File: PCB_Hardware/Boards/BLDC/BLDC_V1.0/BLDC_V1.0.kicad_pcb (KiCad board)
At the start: 4 copper layers, 60 x 60 mm, 180 parts, among them J1 Conn_01x04_Pin, J11 GT-USB-7010ASV, J14 47053-1000, J2 Conn_01x04_Pin, J3 Conn_01x02_Pin, J4 Conn_01x02_Pin, J5 Conn_01x02_Socket, J6 Conn_01x02_Socket, J7 Conn_ARM_SWD_TagConnect_TC2030, J8 Conn_02x06_Odd_Even, J9 Conn_01x06_Socket, Q1 SI2302, Q10 BC847, Q11 BSS138, Q12 BSS84, Q13 IPT015N10N5, Q14 SI2302, Q2 IPT015N10N5, Q3 TPH3R70APL, Q4 TPH3R70APL, Q5 TPH3R70APL, Q6 TPH3R70APL, Q7 TPH3R70APL, Q8 TPH3R70APL, Q9 TPH3R70APL, U1 DRV8353SRTAR, U10 TPD2E2U06DCK, U11 AMS1117-3.3, U12 LM66100DCK, U13 LM66100DCK, U14 SRV05-4, U15 TS5A3159ADBVR, U16 CAT24C512C8UTR, U2 MT6835GT-STD, U3 TCAN1044VDR, U5 LM5069MM-2, U6 TLV70233_SOT23-5, U7 STM32G474RET6, U8 SRV05-4, U9 SRV05-4, Y2 XXGBBCNANF-25.000000MHZ

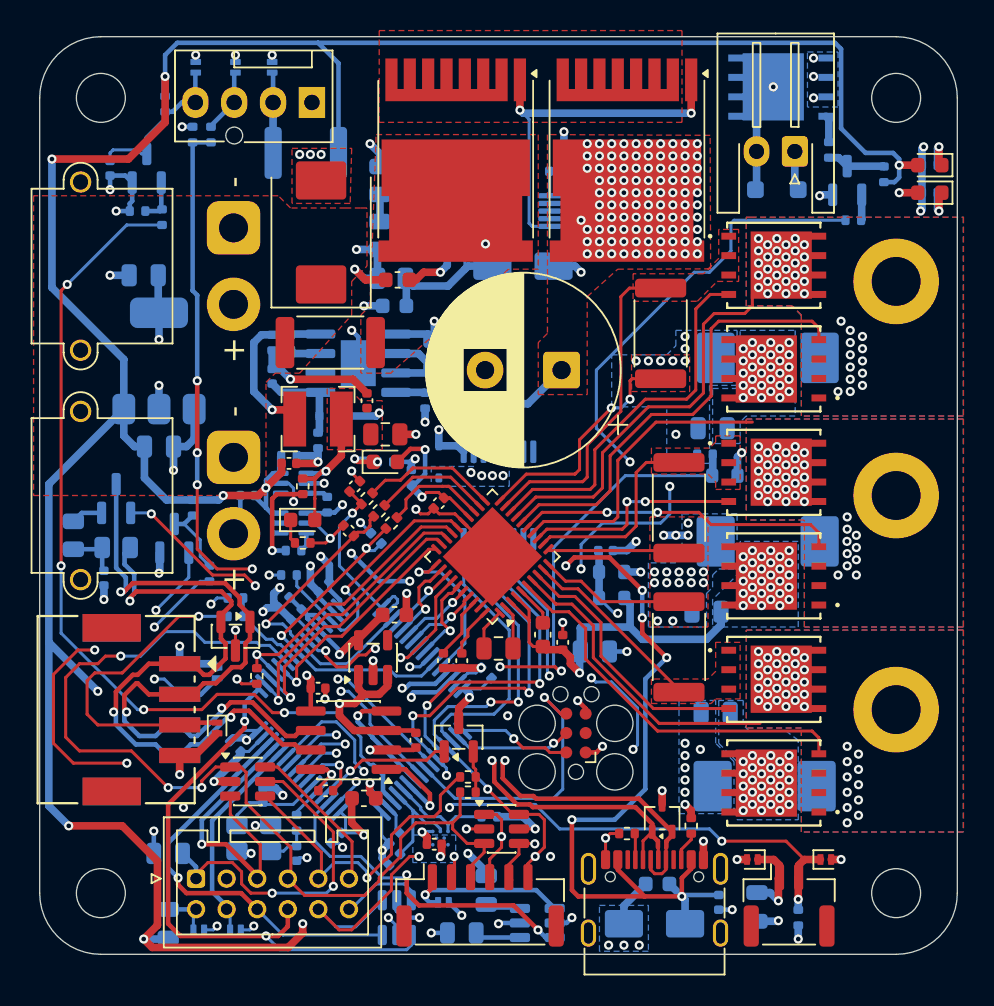
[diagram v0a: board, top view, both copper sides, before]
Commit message: minor BLDC changes and production files for ordering
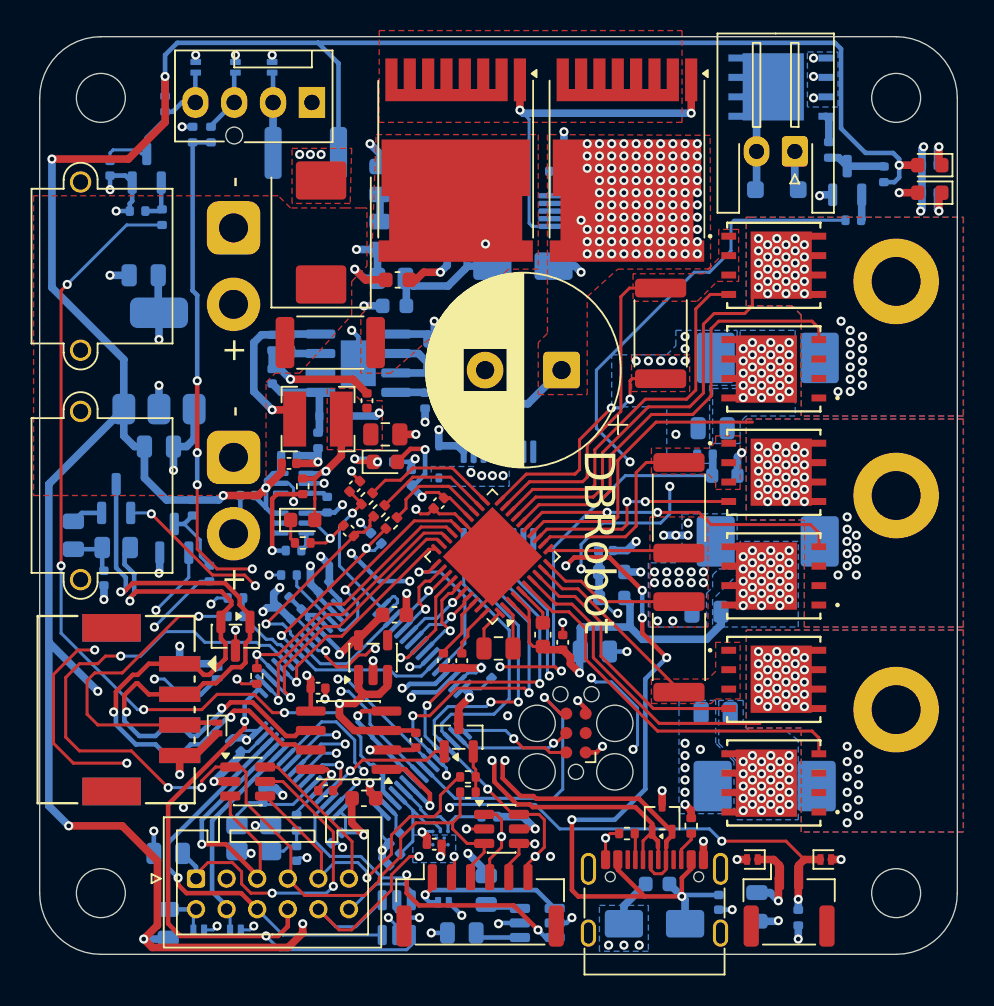
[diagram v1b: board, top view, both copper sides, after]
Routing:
- net GND: track 189.4 -> 184.5 mm
- net /CANFD/CAN+: track 42.2 -> 38.8 mm
- net /CANFD/CAN-: track 46.9 -> 44.1 mm
- net Net-(D17-K): track 28.6 -> 25.9 mm
- net Net-(D5-A): track 7.20 -> 5.55 mm, vias 1 -> 0
- net /GPIO/PC4/SCL/ADC: track 64.6 -> 63.6 mm
- net /Encoder/ENCODER_MISO: track 70.0 -> 69.2 mm
- net +BATT: track 46.0 -> 45.3 mm
- net Net-(D14-K): track 11.6 -> 10.9 mm
- net /Encoder/ENCODER_SCLK: track 56.3 -> 55.7 mm
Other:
- board text added: "DBRobot"
